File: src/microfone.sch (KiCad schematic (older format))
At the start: 4 parts

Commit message: Substituição dos transitores NMOS pelo transistor 2n7000
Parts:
- removed Q?: MMBF170, SOT-23, symbol MMBF170
- added Q?: 2n7000, symbol Q_NMOS_DGS
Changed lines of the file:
@@
 $Descr A4 11693 8268
 encoding utf-8
-Sheet 4 5
+Sheet 5 5
 Title "Circuito do microfone"
 Date "2016-08-28"
@@
 $EndComp
 Wire Wire Line
-	5400 3450 5400 3300
+	5400 3250 5400 3450
 Wire Wire Line
-	5050 3450 5400 3450
-$Comp
-L MMBF170 Q?
-U 1 1 57CE1690
-P 5600 3250
-F 0 "Q?" H 5800 3325 50  0000 L CNN
-F 1 "MMBF170" H 5800 3250 50  0000 L CNN
-F 2 "SOT-23" H 5800 3175 50  0000 L CIN
-F 3 "" H 5600 3250 50  0000 L CNN
-	1    5600 3250
-	1    0    0    -1
-$EndComp
+	5400 3450 5050 3450
 $Comp
 L MIC_ELECTRET U?
@@
 Text HLabel 7050 3000 2    60   UnSpc ~ 0
 MIC_ANALOG_OUT
+$Comp
+L Q_NMOS_DGS Q?
+U 1 1 57D1783F
+P 5600 3250
+F 0 "Q?" H 5900 3300 50  0000 R CNN
+F 1 "2n7000" H 6250 3200 50  0000 R CNN
+F 2 "" H 5800 3350 50  0000 C CNN
+F 3 "" H 5600 3250 50  0000 C CNN
+	1    5600 3250
+	1    0    0    -1
+$EndComp
 $EndSCHEMATC

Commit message: Verificação ERC -- checagem de erros elétricos no esquema -- concluída com sucesso. Há apenas dois warnings que não indicam problemas.
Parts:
- gave numbers to parts that had none: 4
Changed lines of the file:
@@
 	5900 3000 5700 3000
 $Comp
-L C C?
+L C C6
 U 1 1 57CE168C
 P 6050 3000
-F 0 "C?" H 6075 3100 50  0000 L CNN
+F 0 "C6" H 6075 3100 50  0000 L CNN
 F 1 "10u" H 6075 2900 50  0000 L CNN
 F 2 "" H 6088 2850 50  0000 C CNN
@@
 $EndComp
 $Comp
-L +12V #PWR?
+L +12V #PWR027
 U 1 1 57CE168D
 P 5700 2400
-F 0 "#PWR?" H 5700 2250 50  0001 C CNN
+F 0 "#PWR027" H 5700 2250 50  0001 C CNN
 F 1 "+12V" H 5700 2540 50  0000 C CNN
 F 2 "" H 5700 2400 50  0000 C CNN
@@
 	5700 3050 5700 2900
 $Comp
-L R R?
+L R R34
 U 1 1 57CE168E
 P 5700 2750
-F 0 "R?" V 5780 2750 50  0000 C CNN
+F 0 "R34" V 5780 2750 50  0000 C CNN
 F 1 "10000" V 5700 2750 50  0000 C CNN
 F 2 "" V 5630 2750 50  0000 C CNN
@@
 $EndComp
 Wire Wire Line
-	5700 3450 5700 3650
-Wire Wire Line
 	5050 3650 5800 3650
 Wire Wire Line
 	5800 3650 5800 3950
 $Comp
-L GND #PWR?
+L GND #PWR028
 U 1 1 57CE168F
 P 5800 3950
-F 0 "#PWR?" H 5800 3700 50  0001 C CNN
+F 0 "#PWR028" H 5800 3700 50  0001 C CNN
 F 1 "GND" H 5800 3800 50  0000 C CNN
 F 2 "" H 5800 3950 50  0000 C CNN
@@
 	5400 3450 5050 3450
 $Comp
-L MIC_ELECTRET U?
+L MIC_ELECTRET U4
 U 1 1 57CE1691
 P 4750 3550
-F 0 "U?" H 4750 3800 60  0000 C CNN
+F 0 "U4" H 4750 3800 60  0000 C CNN
 F 1 "MIC_ELECTRET" H 4750 3200 60  0000 C CNN
 F 2 "" H 4750 3550 60  0000 C CNN
@@
 MIC_ANALOG_OUT
 $Comp
-L Q_NMOS_DGS Q?
+L Q_NMOS_DGS Q3
 U 1 1 57D1783F
 P 5600 3250
-F 0 "Q?" H 5900 3300 50  0000 R CNN
+F 0 "Q3" H 5900 3300 50  0000 R CNN
 F 1 "2n7000" H 6250 3200 50  0000 R CNN
 F 2 "" H 5800 3350 50  0000 C CNN
@@
 	1    0    0    -1
 $EndComp
+Wire Wire Line
+	5700 3450 5700 3650
+Connection ~ 5700 3650
 $EndSCHEMATC

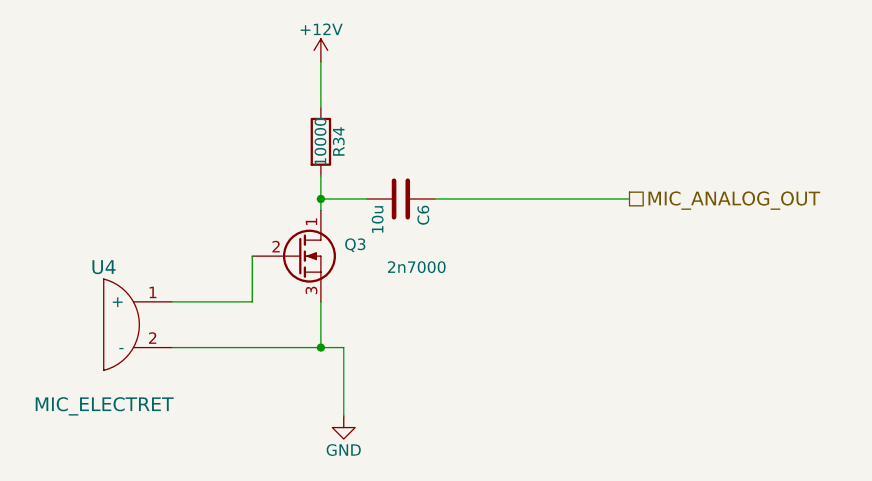
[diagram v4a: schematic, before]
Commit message: Footprint atualizado
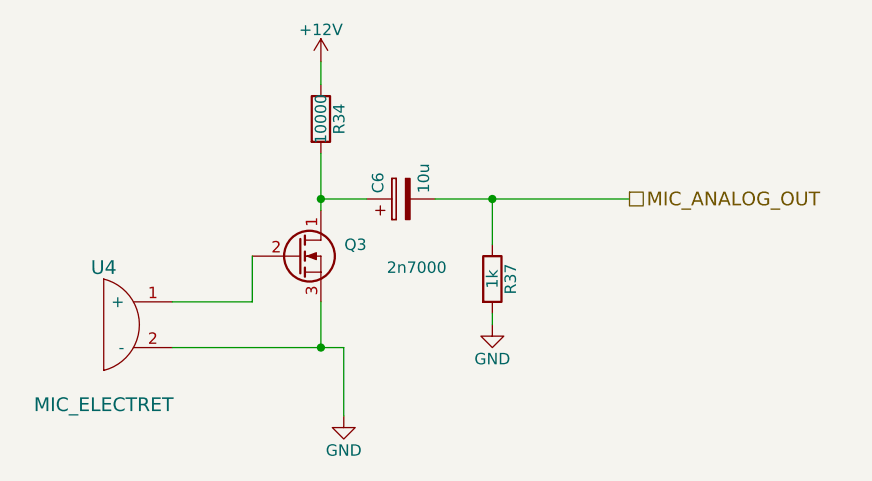
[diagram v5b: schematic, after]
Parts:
- removed C6: 10u, symbol C
- added C6: 10u, Capacitores:Cap_Eletrolitico_8x3.5, symbol CP
- added R37: 1k, Resistors_ThroughHole:Resistor_Horizontal_RM7mm, symbol R
- Q3: footprint (none) -> TO_SOT_Packages_THT:TO-92_Inline_Narrow_Oval
- R34: footprint (none) -> Resistors_ThroughHole:Resistor_Horizontal_RM7mm
- U4: footprint (none) -> Capacitors_ThroughHole:C_Radial_D10_L20_P2.5
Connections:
- net GND: now also R37.2
- net MIC_ANALOG_OUT: now also C6.2, R37.1
- net at Q3.1 (D), R34.2: now also C6.1
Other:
- moved on the sheet: R34
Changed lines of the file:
@@
 Comment4 ""
 $EndDescr
-Wire Wire Line
-	6200 3000 7050 3000
-Connection ~ 5700 3000
-Wire Wire Line
-	5900 3000 5700 3000
-$Comp
-L C C6
-U 1 1 57CE168C
-P 6050 3000
-F 0 "C6" H 6075 3100 50  0000 L CNN
-F 1 "10u" H 6075 2900 50  0000 L CNN
-F 2 "" H 6088 2850 50  0000 C CNN
-F 3 "" H 6050 3000 50  0000 C CNN
-	1    6050 3000
-	0    1    1    0
-$EndComp
 $Comp
 L +12V #PWR027
@@
 	1    0    0    -1
 $EndComp
-Wire Wire Line
-	5700 2600 5700 2400
-Wire Wire Line
-	5700 3050 5700 2900
 $Comp
 L R R34
 U 1 1 57CE168E
-P 5700 2750
-F 0 "R34" V 5780 2750 50  0000 C CNN
-F 1 "10000" V 5700 2750 50  0000 C CNN
-F 2 "" V 5630 2750 50  0000 C CNN
-F 3 "" H 5700 2750 50  0000 C CNN
-	1    5700 2750
+P 5700 2650
+F 0 "R34" V 5780 2650 50  0000 C CNN
+F 1 "10000" V 5700 2650 50  0000 C CNN
+F 2 "Resistors_ThroughHole:Resistor_Horizontal_RM7mm" V 5630 2650 50  0001 C CNN
+F 3 "" H 5700 2650 50  0000 C CNN
+	1    5700 2650
 	1    0    0    -1
 $EndComp
-Wire Wire Line
-	5050 3650 5800 3650
-Wire Wire Line
-	5800 3650 5800 3950
 $Comp
 L GND #PWR028
@@
 	1    0    0    -1
 $EndComp
-Wire Wire Line
-	5400 3250 5400 3450
-Wire Wire Line
-	5400 3450 5050 3450
 $Comp
 L MIC_ELECTRET U4
@@
 F 0 "U4" H 4750 3800 60  0000 C CNN
 F 1 "MIC_ELECTRET" H 4750 3200 60  0000 C CNN
-F 2 "" H 4750 3550 60  0000 C CNN
+F 2 "Capacitors_ThroughHole:C_Radial_D10_L20_P2.5" H 4750 3550 60  0001 C CNN
 F 3 "" H 4750 3550 60  0000 C CNN
 	1    4750 3550
@@
 F 0 "Q3" H 5900 3300 50  0000 R CNN
 F 1 "2n7000" H 6250 3200 50  0000 R CNN
-F 2 "" H 5800 3350 50  0000 C CNN
+F 2 "TO_SOT_Packages_THT:TO-92_Inline_Narrow_Oval" H 5800 3350 50  0001 C CNN
 F 3 "" H 5600 3250 50  0000 C CNN
 	1    5600 3250
 	1    0    0    -1
 $EndComp
+$Comp
+L CP C6
+U 1 1 57D2AB5E
+P 6050 3000
+F 0 "C6" H 6075 3100 50  0000 L CNN
+F 1 "10u" H 6075 2900 50  0000 L CNN
+F 2 "Capacitores:Cap_Eletrolitico_8x3.5" H 6088 2850 50  0001 C CNN
+F 3 "" H 6050 3000 50  0000 C CNN
+	1    6050 3000
+	0    -1   -1   0
+$EndComp
+$Comp
+L GND #PWR029
+U 1 1 57D2AD46
+P 6450 3550
+F 0 "#PWR029" H 6450 3300 50  0001 C CNN
+F 1 "GND" H 6450 3400 50  0000 C CNN
+F 2 "" H 6450 3550 50  0000 C CNN
+F 3 "" H 6450 3550 50  0000 C CNN
+	1    6450 3550
+	1    0    0    -1
+$EndComp
+Wire Wire Line
+	6200 3000 7050 3000
+Connection ~ 5700 3000
+Wire Wire Line
+	5900 3000 5700 3000
+Wire Wire Line
+	5700 2800 5700 3050
+Wire Wire Line
+	5050 3650 5800 3650
+Wire Wire Line
+	5800 3650 5800 3950
+Wire Wire Line
+	5400 3250 5400 3450
+Wire Wire Line
+	5400 3450 5050 3450
 Wire Wire Line
 	5700 3450 5700 3650
 Connection ~ 5700 3650
+Wire Wire Line
+	5700 2500 5700 2400
+$Comp
+L R R37
+U 1 1 57D2AF52
+P 6450 3350
+F 0 "R37" V 6530 3350 50  0000 C CNN
+F 1 "1k" V 6450 3350 50  0000 C CNN
+F 2 "Resistors_ThroughHole:Resistor_Horizontal_RM7mm" V 6380 3350 50  0001 C CNN
+F 3 "" H 6450 3350 50  0000 C CNN
+	1    6450 3350
+	1    0    0    -1
+$EndComp
+Wire Wire Line
+	6450 3550 6450 3500
+Wire Wire Line
+	6450 3200 6450 3000
+Connection ~ 6450 3000
 $EndSCHEMATC

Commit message: Removi circuito de microfone e coloquei conector de 6 pinos, além de um resistor para proteção. O conector pode ser invertido sem problemas de danos à placa. Há um novo projeto dentro da pasta placa_microfone, referente à placa externa de captura do microfone a ser conectada.
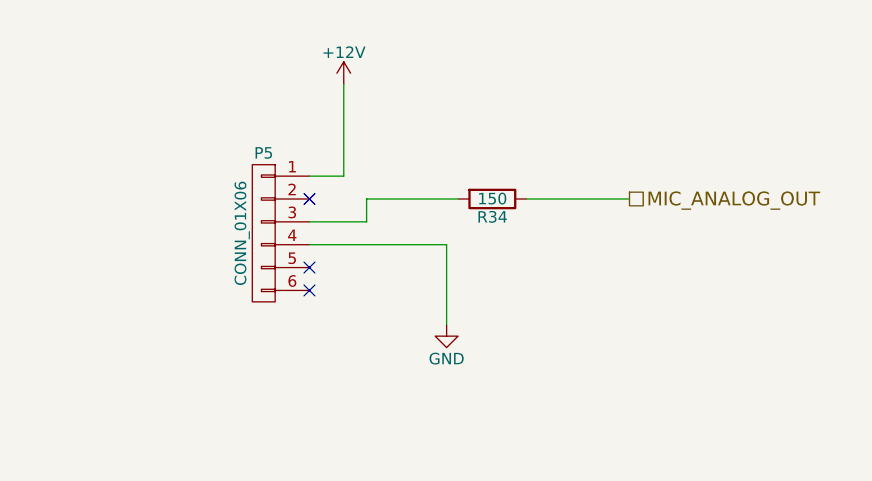
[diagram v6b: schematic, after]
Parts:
- removed C6: 10u, Capacitores:Cap_Eletrolitico_8x3.5, symbol CP
- removed Q3: 2n7000, TO_SOT_Packages_THT:TO-92_Inline_Narrow_Oval, symbol Q_NMOS_DGS
- removed R37: 1k, Resistors_ThroughHole:Resistor_Horizontal_RM7mm, symbol R
- removed U4: MIC_ELECTRET, Capacitors_ThroughHole:C_Radial_D10_L20_P2.5, symbol MIC_ELECTRET
- added P5: CONN_01X06, Connect:Wafer_Vertical17.5x5.8x7RM2.5-6, symbol CONN_01X06
- R34: value 10000 -> 150
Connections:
- net +12V: now also P5.1 (P1); no longer R34.1
- net GND: now also P5.4 (P4)
- net MIC_ANALOG_OUT: now also R34.1
- net at R34.2: now also P5.3 (P3)
- no-connect marks 0 -> 3
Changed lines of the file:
@@
 LIBS:contrib
 LIBS:valves
-LIBS:L293D
-LIBS:ESP8266
 LIBS:poplock_v1-cache
 EELAYER 25 0
@@
 Comment4 ""
 $EndDescr
-$Comp
-L +12V #PWR027
-U 1 1 57CE168D
-P 5700 2400
-F 0 "#PWR027" H 5700 2250 50  0001 C CNN
-F 1 "+12V" H 5700 2540 50  0000 C CNN
-F 2 "" H 5700 2400 50  0000 C CNN
-F 3 "" H 5700 2400 50  0000 C CNN
-	1    5700 2400
-	1    0    0    -1
-$EndComp
-$Comp
-L R R34
-U 1 1 57CE168E
-P 5700 2650
-F 0 "R34" V 5780 2650 50  0000 C CNN
-F 1 "10000" V 5700 2650 50  0000 C CNN
-F 2 "Resistors_ThroughHole:Resistor_Horizontal_RM7mm" V 5630 2650 50  0001 C CNN
-F 3 "" H 5700 2650 50  0000 C CNN
-	1    5700 2650
-	1    0    0    -1
-$EndComp
-$Comp
-L GND #PWR028
-U 1 1 57CE168F
-P 5800 3950
-F 0 "#PWR028" H 5800 3700 50  0001 C CNN
-F 1 "GND" H 5800 3800 50  0000 C CNN
-F 2 "" H 5800 3950 50  0000 C CNN
-F 3 "" H 5800 3950 50  0000 C CNN
-	1    5800 3950
-	1    0    0    -1
-$EndComp
-$Comp
-L MIC_ELECTRET U4
-U 1 1 57CE1691
-P 4750 3550
-F 0 "U4" H 4750 3800 60  0000 C CNN
-F 1 "MIC_ELECTRET" H 4750 3200 60  0000 C CNN
-F 2 "Capacitors_ThroughHole:C_Radial_D10_L20_P2.5" H 4750 3550 60  0001 C CNN
-F 3 "" H 4750 3550 60  0000 C CNN
-	1    4750 3550
-	1    0    0    -1
-$EndComp
 Text HLabel 7050 3000 2    60   UnSpc ~ 0
 MIC_ANALOG_OUT
 $Comp
-L Q_NMOS_DGS Q3
-U 1 1 57D1783F
-P 5600 3250
-F 0 "Q3" H 5900 3300 50  0000 R CNN
-F 1 "2n7000" H 6250 3200 50  0000 R CNN
-F 2 "TO_SOT_Packages_THT:TO-92_Inline_Narrow_Oval" H 5800 3350 50  0001 C CNN
-F 3 "" H 5600 3250 50  0000 C CNN
-	1    5600 3250
-	1    0    0    -1
+L R R34
+U 1 1 57E3E7B4
+P 6450 3000
+F 0 "R34" V 6530 3000 50  0000 C CNN
+F 1 "150" V 6450 3000 50  0000 C CNN
+F 2 "Resistors_ThroughHole:Resistor_Horizontal_RM7mm" V 6380 3000 50  0001 C CNN
+F 3 "" H 6450 3000 50  0000 C CNN
+	1    6450 3000
+	0    1    1    0
 $EndComp
 $Comp
-L CP C6
-U 1 1 57D2AB5E
-P 6050 3000
-F 0 "C6" H 6075 3100 50  0000 L CNN
-F 1 "10u" H 6075 2900 50  0000 L CNN
-F 2 "Capacitores:Cap_Eletrolitico_8x3.5" H 6088 2850 50  0001 C CNN
-F 3 "" H 6050 3000 50  0000 C CNN
-	1    6050 3000
-	0    -1   -1   0
-$EndComp
-$Comp
-L GND #PWR029
-U 1 1 57D2AD46
-P 6450 3550
-F 0 "#PWR029" H 6450 3300 50  0001 C CNN
-F 1 "GND" H 6450 3400 50  0000 C CNN
-F 2 "" H 6450 3550 50  0000 C CNN
-F 3 "" H 6450 3550 50  0000 C CNN
-	1    6450 3550
+L GND #PWR027
+U 1 1 57E3E835
+P 6250 3550
+F 0 "#PWR027" H 6250 3300 50  0001 C CNN
+F 1 "GND" H 6250 3400 50  0000 C CNN
+F 2 "" H 6250 3550 50  0000 C CNN
+F 3 "" H 6250 3550 50  0000 C CNN
+	1    6250 3550
 	1    0    0    -1
 $EndComp
 Wire Wire Line
-	6200 3000 7050 3000
-Connection ~ 5700 3000
+	6300 3000 5900 3000
 Wire Wire Line
-	5900 3000 5700 3000
-Wire Wire Line
-	5700 2800 5700 3050
-Wire Wire Line
-	5050 3650 5800 3650
-Wire Wire Line
-	5800 3650 5800 3950
-Wire Wire Line
-	5400 3250 5400 3450
-Wire Wire Line
-	5400 3450 5050 3450
-Wire Wire Line
-	5700 3450 5700 3650
-Connection ~ 5700 3650
-Wire Wire Line
-	5700 2500 5700 2400
+	6600 3000 7050 3000
 $Comp
-L R R37
-U 1 1 57D2AF52
-P 6450 3350
-F 0 "R37" V 6530 3350 50  0000 C CNN
-F 1 "1k" V 6450 3350 50  0000 C CNN
-F 2 "Resistors_ThroughHole:Resistor_Horizontal_RM7mm" V 6380 3350 50  0001 C CNN
-F 3 "" H 6450 3350 50  0000 C CNN
-	1    6450 3350
+L CONN_01X06 P5
+U 1 1 57E3EA18
+P 5450 3150
+F 0 "P5" H 5450 3500 50  0000 C CNN
+F 1 "CONN_01X06" V 5550 3150 50  0000 C CNN
+F 2 "Connect:Wafer_Vertical17.5x5.8x7RM2.5-6" H 5450 3150 50  0001 C CNN
+F 3 "" H 5450 3150 50  0000 C CNN
+	1    5450 3150
+	-1   0    0    -1
+$EndComp
+$Comp
+L +12V #PWR028
+U 1 1 57E3EAC4
+P 5800 2500
+F 0 "#PWR028" H 5800 2350 50  0001 C CNN
+F 1 "+12V" H 5800 2640 50  0000 C CNN
+F 2 "" H 5800 2500 50  0000 C CNN
+F 3 "" H 5800 2500 50  0000 C CNN
+	1    5800 2500
 	1    0    0    -1
 $EndComp
 Wire Wire Line
-	6450 3550 6450 3500
+	5800 2500 5800 2900
 Wire Wire Line
-	6450 3200 6450 3000
-Connection ~ 6450 3000
+	5800 2900 5650 2900
+Wire Wire Line
+	5650 3200 6250 3200
+Wire Wire Line
+	6250 3200 6250 3550
+Wire Wire Line
+	5650 3100 5900 3100
+Wire Wire Line
+	5900 3100 5900 3000
+NoConn ~ 5650 3000
+NoConn ~ 5650 3300
+NoConn ~ 5650 3400
 $EndSCHEMATC
